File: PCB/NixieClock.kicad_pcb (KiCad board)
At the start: 2 copper layers, 146.7 x 95.2 mm, 49 parts, among them J1 12V, J3 Conn_01x03_Male, J4 Conn_01x03_Male, Q1 MPSA42, Q2 MPSA42, Q3 MPSA42, Q4 MPSA42, U1 L7805, U10 74141, U11 74141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

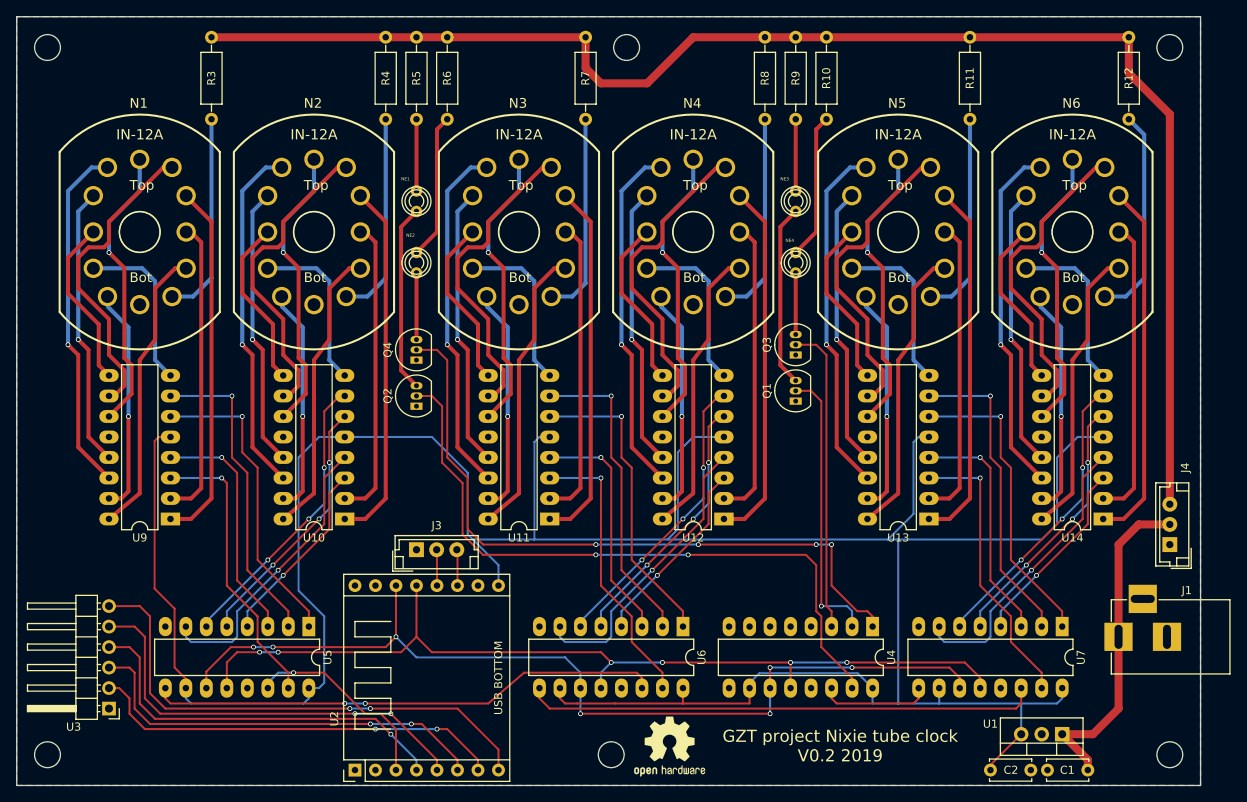
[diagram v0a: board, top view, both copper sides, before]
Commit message: PCB top fill
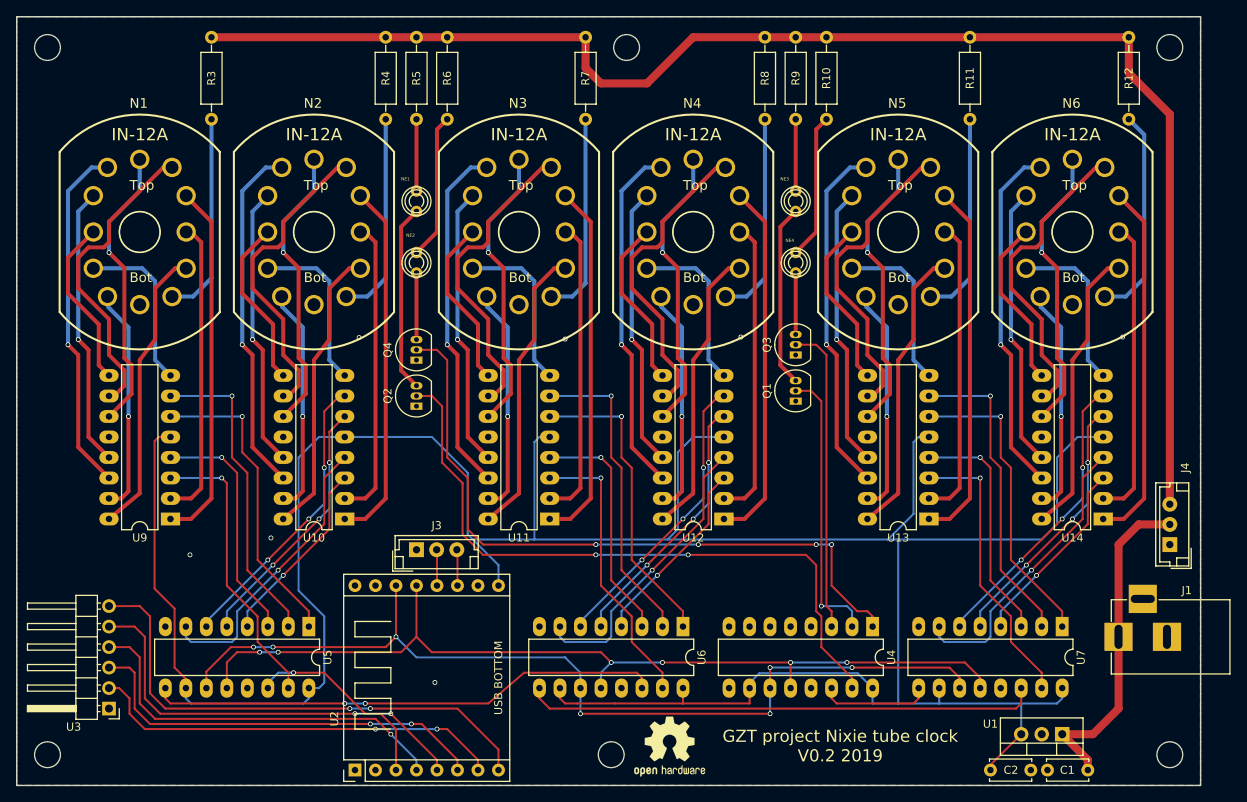
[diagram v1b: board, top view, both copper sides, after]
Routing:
- net GND: vias 0 -> 7
- added copper zone on F.Cu, net GND
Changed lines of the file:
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@@
-(kicad_pcb (version 4) (host pcbnew 4.0.7-e2-6376~61~ubuntu18.04.1)
+(kicad_pcb (version 20171130) (host pcbnew 5.1.5-52549c5~84~ubuntu18.04.1)
   (general
-    (links 175)
-    (no_connects 0)
-    (area 67.612857 28.415 249.785 140.195)
     (thickness 1.6)
     (drawings 8)
-    (tracks 929)
+    (tracks 936)
     (zones 0)
     (modules 49)
@@
     (zone_45_only no)
     (trace_min 0.2)
-    (segment_width 0.2)
-    (edge_width 0.15)
     (via_size 0.6)
     (via_drill 0.4)
@@
     (uvia_min_size 0.2)
     (uvia_min_drill 0.1)
+    (edge_width 0.15)
+    (segment_width 0.2)
     (pcb_text_width 0.3)
     (pcb_text_size 1.5 1.5)
@@
       (layerselection 0x010f0_80000001)
       (usegerberextensions true)
+      (usegerberattributes false)
+      (usegerberadvancedattributes false)
+      (creategerberjobfile false)
       (excludeedgelayer true)
       (linewidth 0.100000)
@@
       (hpglpennumber 1)
       (hpglpenspeed 20)
-      (hpglpendiameter 15)
-      (hpglpenoverlay 2)
+      (hpglpendiameter 15.000000)
       (psnegative false)
       (psa4output false)
@@
       (drillshape 0)
       (scaleselection 1)
-      (outputdirectory /media/gapi/Data/dev/KiCad/NixieClock/Export/))
+      (outputdirectory "/media/gapi/Data/dev/KiCad/NixieClock/Export/"))
   )
   (net 0 "")
@@
       (net 2 GND))
     (model ${KISYS3DMOD}/TO_SOT_Packages_THT.3dshapes/TO-92_Inline_Narrow_Oval.wrl
-      (at (xyz 0.05 0 0))
+      (offset (xyz 1.269999980926514 0 0))
       (scale (xyz 1 1 1))
       (rotate (xyz 0 0 -90))
@@
       (net 2 GND))
     (model ${KISYS3DMOD}/TO_SOT_Packages_THT.3dshapes/TO-92_Inline_Narrow_Oval.wrl
-      (at (xyz 0.05 0 0))
+      (offset (xyz 1.269999980926514 0 0))
       (scale (xyz 1 1 1))
       (rotate (xyz 0 0 -90))
@@
       (net 2 GND))
     (model ${KISYS3DMOD}/TO_SOT_Packages_THT.3dshapes/TO-92_Inline_Narrow_Oval.wrl
-      (at (xyz 0.05 0 0))
+      (offset (xyz 1.269999980926514 0 0))
       (scale (xyz 1 1 1))
       (rotate (xyz 0 0 -90))
@@
       (net 2 GND))
     (model ${KISYS3DMOD}/TO_SOT_Packages_THT.3dshapes/TO-92_Inline_Narrow_Oval.wrl
-      (at (xyz 0.05 0 0))
+      (offset (xyz 1.269999980926514 0 0))
       (scale (xyz 1 1 1))
       (rotate (xyz 0 0 -90))
@@
     )
     (fp_text value IN-12A (at 0 -12.065) (layer F.SilkS)
-      (effects (font (thickness 0.15)))
+      (effects (font (size 1.524 1.524) (thickness 0.15)))
     )
     (fp_arc (start 0 1.596433) (end 9.921875 9.921875) (angle 100) (layer F.SilkS) (width 0.254))
@@
     )
     (fp_text value IN-12A (at 0 -12.065) (layer F.SilkS)
-      (effects (font (thickness 0.15)))
+      (effects (font (size 1.524 1.524) (thickness 0.15)))
     )
     (fp_arc (start 0 1.596433) (end 9.921875 9.921875) (angle 100) (layer F.SilkS) (width 0.254))
@@
     )
     (fp_text value IN-12A (at 0 -12.065) (layer F.SilkS)
-      (effects (font (thickness 0.15)))
+      (effects (font (size 1.524 1.524) (thickness 0.15)))
     )
     (fp_arc (start 0 1.596433) (end 9.921875 9.921875) (angle 100) (layer F.SilkS) (width 0.254))
@@
     )
     (fp_text value IN-12A (at 0 -12.065) (layer F.SilkS)
-      (effects (font (thickness 0.15)))
+      (effects (font (size 1.524 1.524) (thickness 0.15)))
     )
     (fp_arc (start 0 1.596433) (end 9.921875 9.921875) (angle 100) (layer F.SilkS) (width 0.254))
@@
     )
     (fp_text value IN-12A (at 0 -12.065) (layer F.SilkS)
-      (effects (font (thickness 0.15)))
+      (effects (font (size 1.524 1.524) (thickness 0.15)))
     )
     (fp_arc (start 0 1.596433) (end 9.921875 9.921875) (angle 100) (layer F.SilkS) (width 0.254))
@@
     )
     (fp_text value IN-12A (at 0 -12.065) (layer F.SilkS)
-      (effects (font (thickness 0.15)))
+      (effects (font (size 1.524 1.524) (thickness 0.15)))
     )
     (fp_arc (start 0 1.596433) (end 9.921875 9.921875) (angle 100) (layer F.SilkS) (width 0.254))
@@
     (descr "DC Barrel Jack")
     (tags "Power Jack")
-    (fp_text reference J1 (at -8.45 5.75 360) (layer F.SilkS)
+    (fp_text reference J1 (at -8.45 5.75) (layer F.SilkS)
       (effects (font (size 1 1) (thickness 0.15)))
     )
@@
       (net 3 +5V))
     (model ${KISYS3DMOD}/TO_SOT_Packages_THT.3dshapes/TO-220-3_Vertical.wrl
-      (at (xyz 0.1 0 0))
+      (offset (xyz 2.539999961853027 0 0))
       (scale (xyz 0.393701 0.393701 0.393701))
       (rotate (xyz 0 0 0))
@@
   (segment (start 203.2 132.08) (end 206.375 135.255) (width 1) (layer F.Cu) (net 1) (status 10))
   (segment (start 206.375 135.255) (end 206.375 136.525) (width 1) (layer F.Cu) (net 1) (status 20))
+  (via (at 125.476 125.6665) (size 0.6) (drill 0.4) (layers F.Cu B.Cu) (net 2))
+  (via (at 95.123 109.855) (size 0.6) (drill 0.4) (layers F.Cu B.Cu) (net 2))
+  (via (at 116.078 82.931) (size 0.6) (drill 0.4) (layers F.Cu B.Cu) (net 2))
+  (via (at 141.605 83.1215) (size 0.6) (drill 0.4) (layers F.Cu B.Cu) (net 2))
+  (via (at 163.3855 82.8675) (size 0.6) (drill 0.4) (layers F.Cu B.Cu) (net 2))
+  (via (at 210.693 82.8675) (size 0.6) (drill 0.4) (layers F.Cu B.Cu) (net 2))
+  (via (at 105.156 107.7595) (size 0.6) (drill 0.4) (layers F.Cu B.Cu) (net 2))
   (segment (start 94.615 126.365) (end 94.615 125.222) (width 0.25) (layer F.Cu) (net 3))
   (segment (start 94.615 125.222) (end 93.218 123.825) (width 0.25) (layer F.Cu) (net 3))
@@
       )
     )
+  )
+  (zone (net 2) (net_name GND) (layer F.Cu) (hatch edge 0.508)
+    (connect_pads thru_hole_only (clearance 0.508))
+    (min_thickness 0.254)
+    (fill yes (arc_segments 16) (thermal_gap 0.508) (thermal_bridge_width 0.508))
+    (polygon
+      (pts
+        (xy 73.688218 138.43) (xy 73.688218 43.18) (xy 220.373218 43.18) (xy 220.373218 138.43)
+      )
+    )

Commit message: Some PCB fixes
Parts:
- moved ? 28.4 mm to (170.4, 110.0)
- moved C1 0.06 mm to (206.4, 136.5)
- moved C2 0.06 mm to (194.2, 136.5)
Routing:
- net GND: vias 7 -> 6
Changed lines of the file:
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@@
     (thickness 1.6)
     (drawings 8)
-    (tracks 936)
+    (tracks 935)
     (zones 0)
     (modules 49)
@@
   )
   (layers
-    (0 F.Cu signal)
-    (31 B.Cu signal)
-    (32 B.Adhes user hide)
+    (0 F.Cu signal hide)
+    (31 B.Cu signal hide)
+    (32 B.Adhes user)
     (33 F.Adhes user hide)
-    (34 B.Paste user hide)
-    (35 F.Paste user hide)
+    (34 B.Paste user)
+    (35 F.Paste user)
     (36 B.SilkS user)
     (37 F.SilkS user)
-    (38 B.Mask user hide)
-    (39 F.Mask user hide)
-    (40 Dwgs.User user hide)
-    (41 Cmts.User user hide)
+    (38 B.Mask user)
+    (39 F.Mask user)
+    (40 Dwgs.User user)
+    (41 Cmts.User user)
     (42 Eco1.User user hide)
     (43 Eco2.User user hide)
     (44 Edge.Cuts user hide)
-    (45 Margin user hide)
+    (45 Margin user)
     (46 B.CrtYd user hide)
-    (47 F.CrtYd user hide)
-    (48 B.Fab user hide)
+    (47 F.CrtYd user)
+    (48 B.Fab user)
     (49 F.Fab user hide)
   )
@@
     (descr "JST EH series connector, B03B-EH-A, 2.50mm pitch, top entry")
     (tags "connector jst eh top vertical straight")
-    (fp_text reference J4 (at 9.525 1.905 90) (layer F.SilkS)
+    (fp_text reference J4 (at 8.8265 1.8415 180) (layer F.SilkS)
       (effects (font (size 1 1) (thickness 0.15)))
     )
@@
   )
   (module Capacitor_THT:C_Disc_D5.0mm_W2.5mm_P5.00mm (layer F.Cu)
-    (at 206.375 136.525 180)
+    (at 206.4385 136.525 180)
     (descr "C, Disc series, Radial, pin pitch=5.00mm, , diameter*width=5*2.5mm^2, Capacitor, http://cdn-reichelt.de/documents/datenblatt/B300/DS_KERKO_TC.pdf")
     (tags "C Disc series Radial pin pitch 5.00mm  diameter 5mm width 2.5mm Capacitor")
@@
   )
   (module Capacitor_THT:C_Disc_D5.0mm_W2.5mm_P5.00mm (layer F.Cu)
-    (at 194.31 136.525)
+    (at 194.2465 136.525)
     (descr "C, Disc series, Radial, pin pitch=5.00mm, , diameter*width=5*2.5mm^2, Capacitor, http://cdn-reichelt.de/documents/datenblatt/B300/DS_KERKO_TC.pdf")
     (tags "C Disc series Radial pin pitch 5.00mm  diameter 5mm width 2.5mm Capacitor")
@@
   )
   (module Symbol:OSHW-Logo2_9.8x8mm_SilkScreen (layer F.Cu)
-    (at 154.559 133.604)
+    (at 170.3705 109.982)
     (descr "Open Source Hardware Symbol")
     (tags "Logo Symbol OSHW")
@@
   (segment (start 203.2 132.08) (end 206.375 135.255) (width 1) (layer F.Cu) (net 1) (status 10))
   (segment (start 206.375 135.255) (end 206.375 136.525) (width 1) (layer F.Cu) (net 1) (status 20))
-  (via (at 125.476 125.6665) (size 0.6) (drill 0.4) (layers F.Cu B.Cu) (net 2))
-  (via (at 95.123 109.855) (size 0.6) (drill 0.4) (layers F.Cu B.Cu) (net 2))
-  (via (at 116.078 82.931) (size 0.6) (drill 0.4) (layers F.Cu B.Cu) (net 2))
-  (via (at 141.605 83.1215) (size 0.6) (drill 0.4) (layers F.Cu B.Cu) (net 2))
-  (via (at 163.3855 82.8675) (size 0.6) (drill 0.4) (layers F.Cu B.Cu) (net 2))
-  (via (at 210.693 82.8675) (size 0.6) (drill 0.4) (layers F.Cu B.Cu) (net 2))
-  (via (at 105.156 107.7595) (size 0.6) (drill 0.4) (layers F.Cu B.Cu) (net 2))
+  (via (at 124.5235 125.6665) (size 0.6) (drill 0.4) (layers F.Cu B.Cu) (net 2))
+  (via (at 95.631 110.5535) (size 0.6) (drill 0.4) (layers F.Cu B.Cu) (net 2))
+  (via (at 209.4865 81.0895) (size 0.6) (drill 0.4) (layers F.Cu B.Cu) (net 2))
+  (via (at 140.589 81.407) (size 0.6) (drill 0.4) (layers F.Cu B.Cu) (net 2))
+  (via (at 162.56 81.661) (size 0.6) (drill 0.4) (layers F.Cu B.Cu) (net 2))
+  (via (at 115.6335 81.661) (size 0.6) (drill 0.4) (layers F.Cu B.Cu) (net 2))
   (segment (start 94.615 126.365) (end 94.615 125.222) (width 0.25) (layer F.Cu) (net 3))
   (segment (start 94.615 125.222) (end 93.218 123.825) (width 0.25) (layer F.Cu) (net 3))
@@
     (polygon
       (pts
-        (xy 73.688218 138.43) (xy 73.688218 43.18) (xy 220.373218 43.18) (xy 220.373218 138.43)
+        (xy 73.68299 138.43) (xy 73.68299 43.18) (xy 220.36799 43.18) (xy 220.36799 138.43)
       )
     )
